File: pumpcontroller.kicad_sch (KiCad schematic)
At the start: 17 parts, among them IC801 LM5060MMX_NOPB, Q801 60V 38A

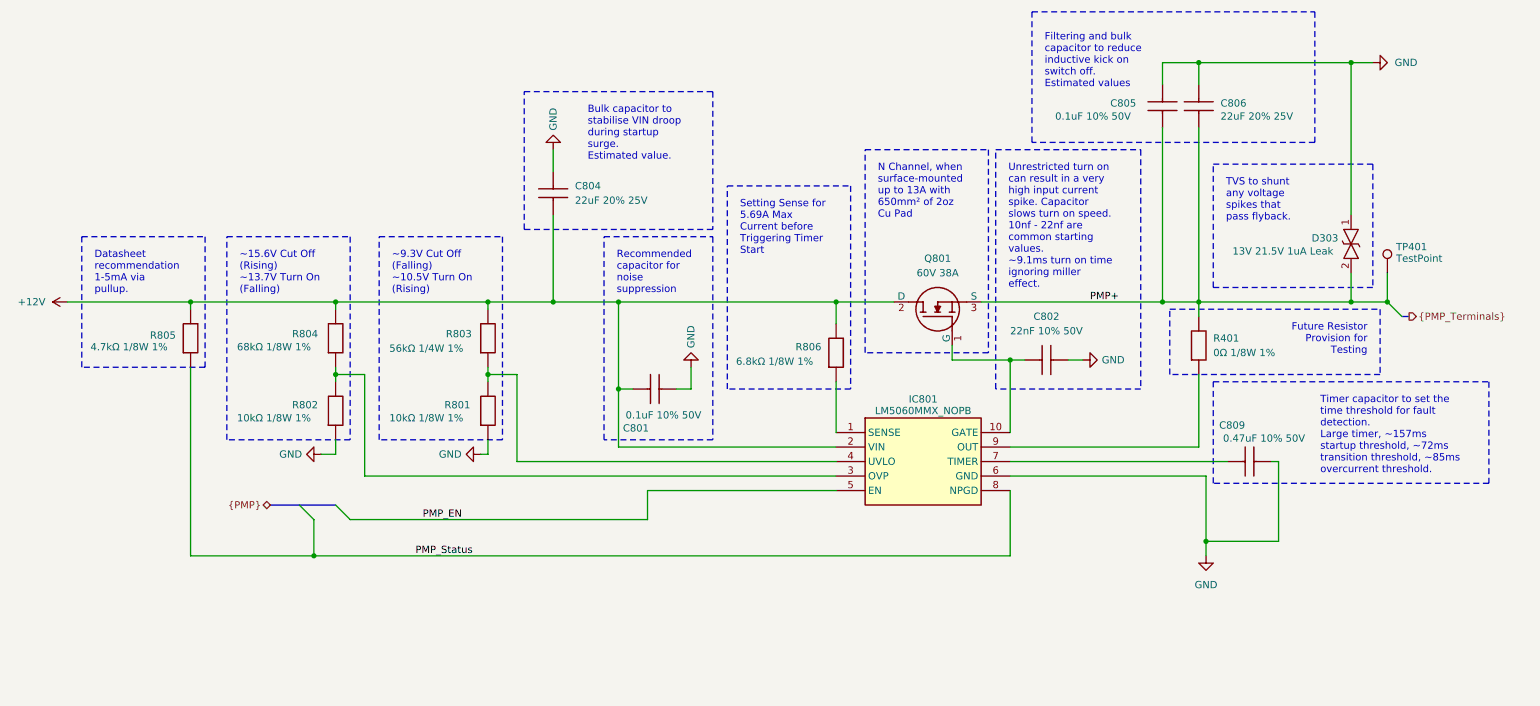
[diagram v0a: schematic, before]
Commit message: Updated schematic, redesigned and included pump pressure switch. Regenerated all outputs.
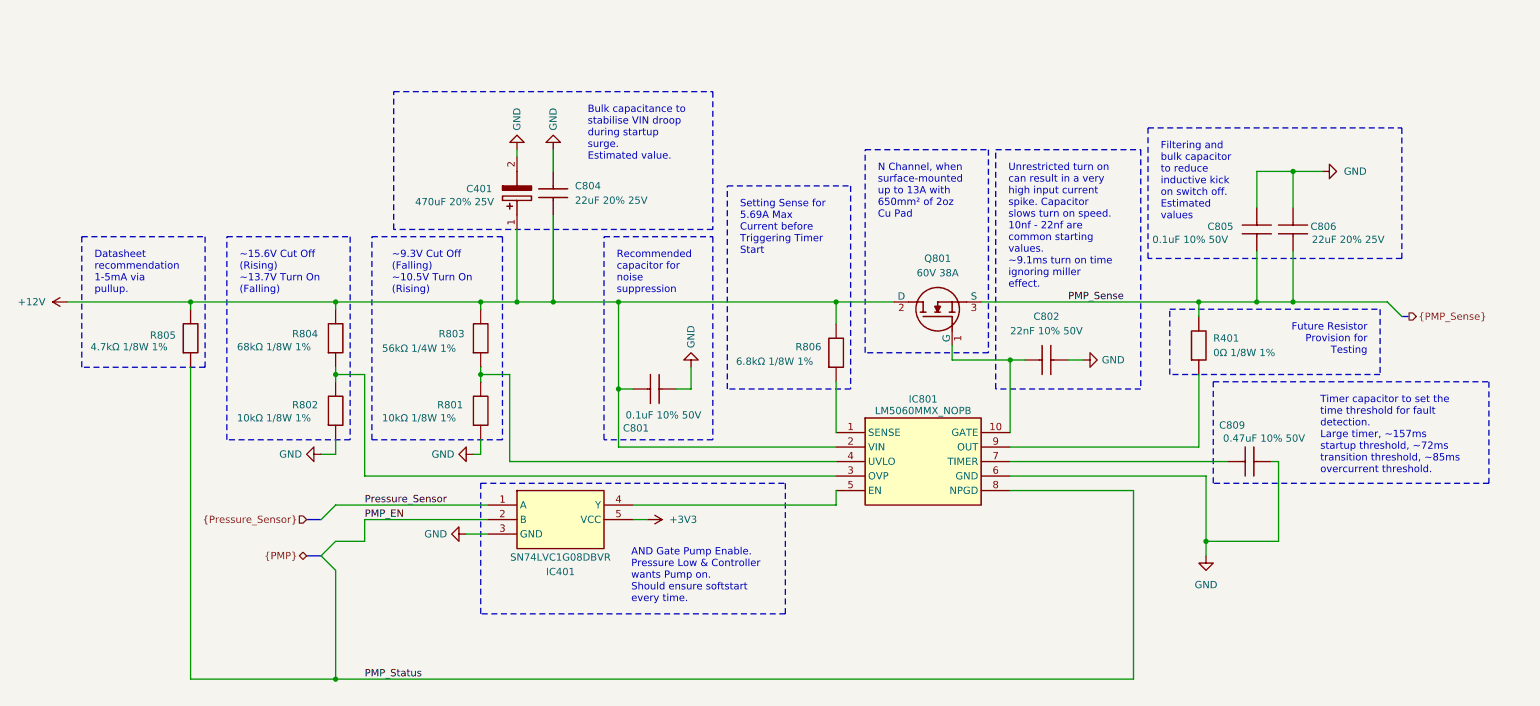
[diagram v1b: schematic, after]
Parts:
- removed D303: 13V 21.5V 1uA Leak, LITTELFUSE Diodes:DO-214AA_Bidirectional, symbol LITTELFUSE Diodes:SMBJ13CA
- removed TP401: TestPoint, TestPoint:TestPoint_Pad_2.0x2.0mm, symbol Connector:TestPoint
- added C401: 470uF 20% 25V, PANASONIC Capacitors:EEEFK1V331P, symbol PANASONIC Capaticitors:EEE-FK1E471P
- added IC401: SN74LVC1G08DBVR, TEXAS INSTRUMENTS ICs:SOT95P280X145-5N, symbol TEXAS INSTRUMENTS ICs:SN74LVC1G08DBVR
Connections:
- net +12V: now also C401.1 (+)
- net GND: now also C401.2 (-), IC401.3 (GND)
- net PMP_EN: now also IC401.2 (B); no longer IC801.5 (EN)
- net PMP+ renamed PMP_Sense
- new net: IC401.4 (Y), IC801.5 (EN)
- new net +3V3: IC401.5 (VCC)
- new net Pressure_Sensor: IC401.1 (A)
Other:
- moved on the sheet: C805, C806, R801, R803

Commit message: Added pull downs on enable lines and regenerated outputs.
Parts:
- added R402, R403: 10kΩ 1/8W 1%, JLCPCB Basic:RESC2013X65N, symbol JLCPCB Basic:0805W8F1002T5E
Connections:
- net GND: now also R402.2, R403.2
- net PMP_EN: now also R403.1
- net Pressure_Sensor: now also R402.1

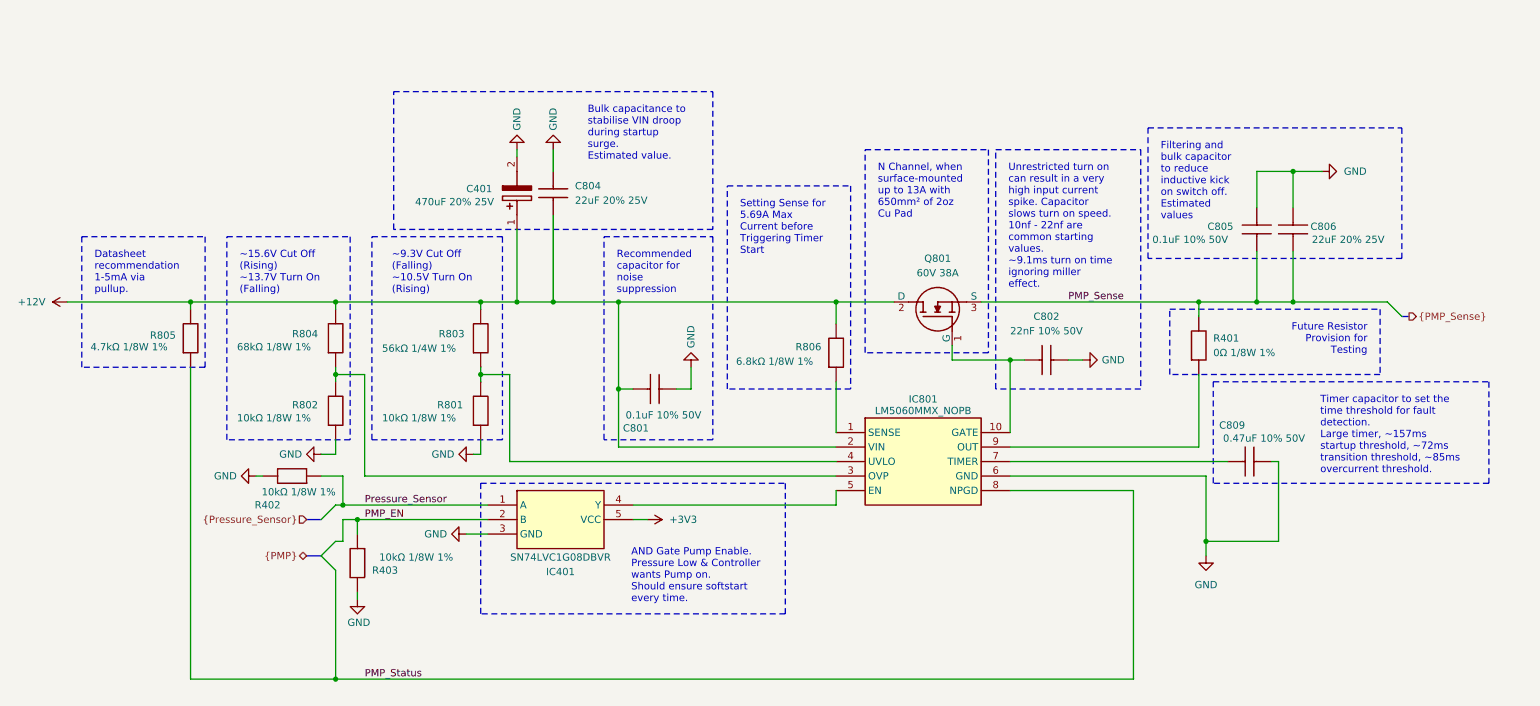
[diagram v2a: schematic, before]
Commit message: Swapped 12v pull up to 3.3v pull up and added 0.1uf cap to AND, then regenerated outputs.
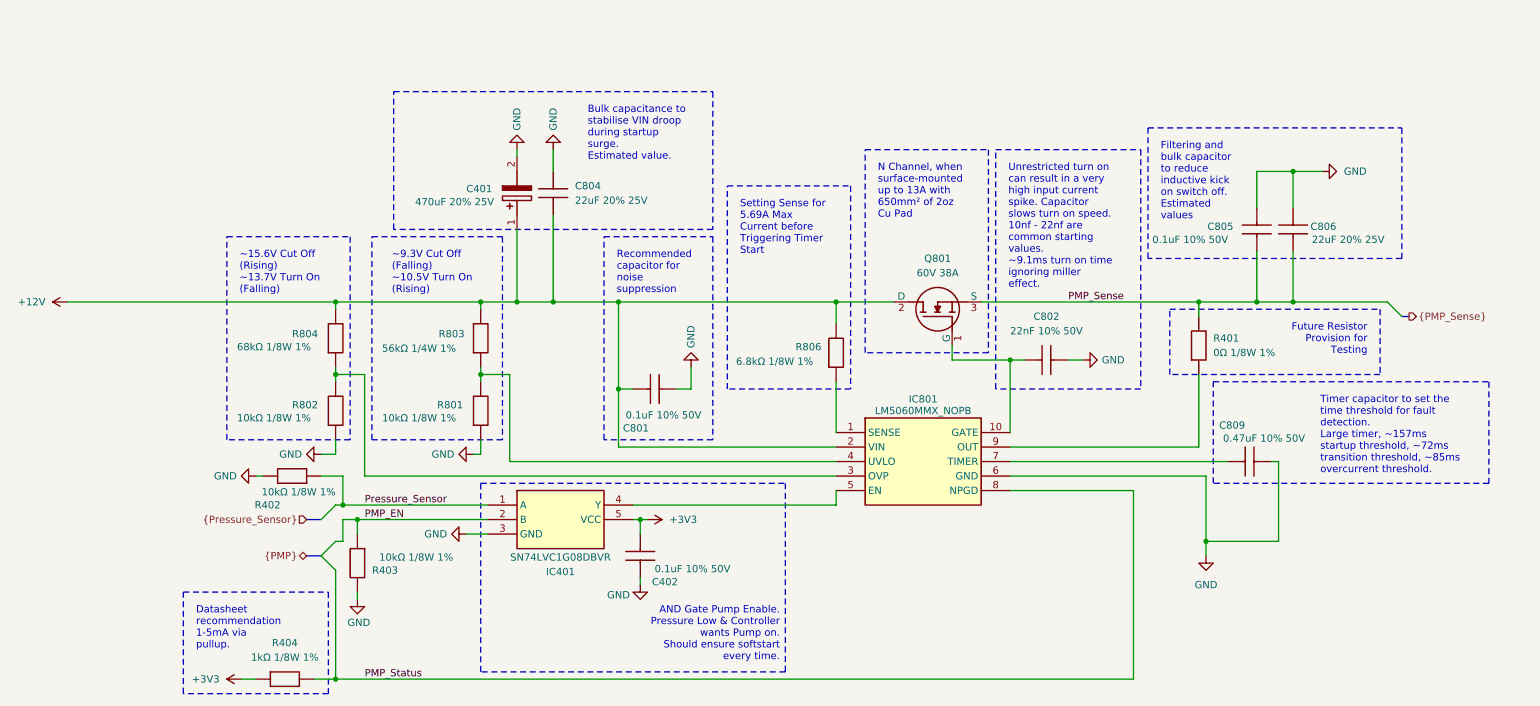
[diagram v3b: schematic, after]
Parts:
- removed R805: 4.7kΩ 1/8W 1%, JLCPCB Basic:RESC2013X65N, symbol JLCPCB Basic:0805W8F4701T5E
- added C402: 0.1uF 10% 50V, JLCPCB Basic:CAPC1608X90N, symbol JLCPCB Basic:CC0603KRX7R9BB104
- added R404: 1kΩ 1/8W 1%, JLCPCB Basic:RESC2013X65N, symbol JLCPCB Basic:0805W8F1001T5E
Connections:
- net +3V3: now also C402.2, R404.1
- net GND: now also C402.1
- net PMP_Status: now also R404.2
